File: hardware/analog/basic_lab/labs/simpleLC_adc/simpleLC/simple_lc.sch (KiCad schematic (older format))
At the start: 5 parts, among them J2 Conn_01x02_Male, Q2 BC547

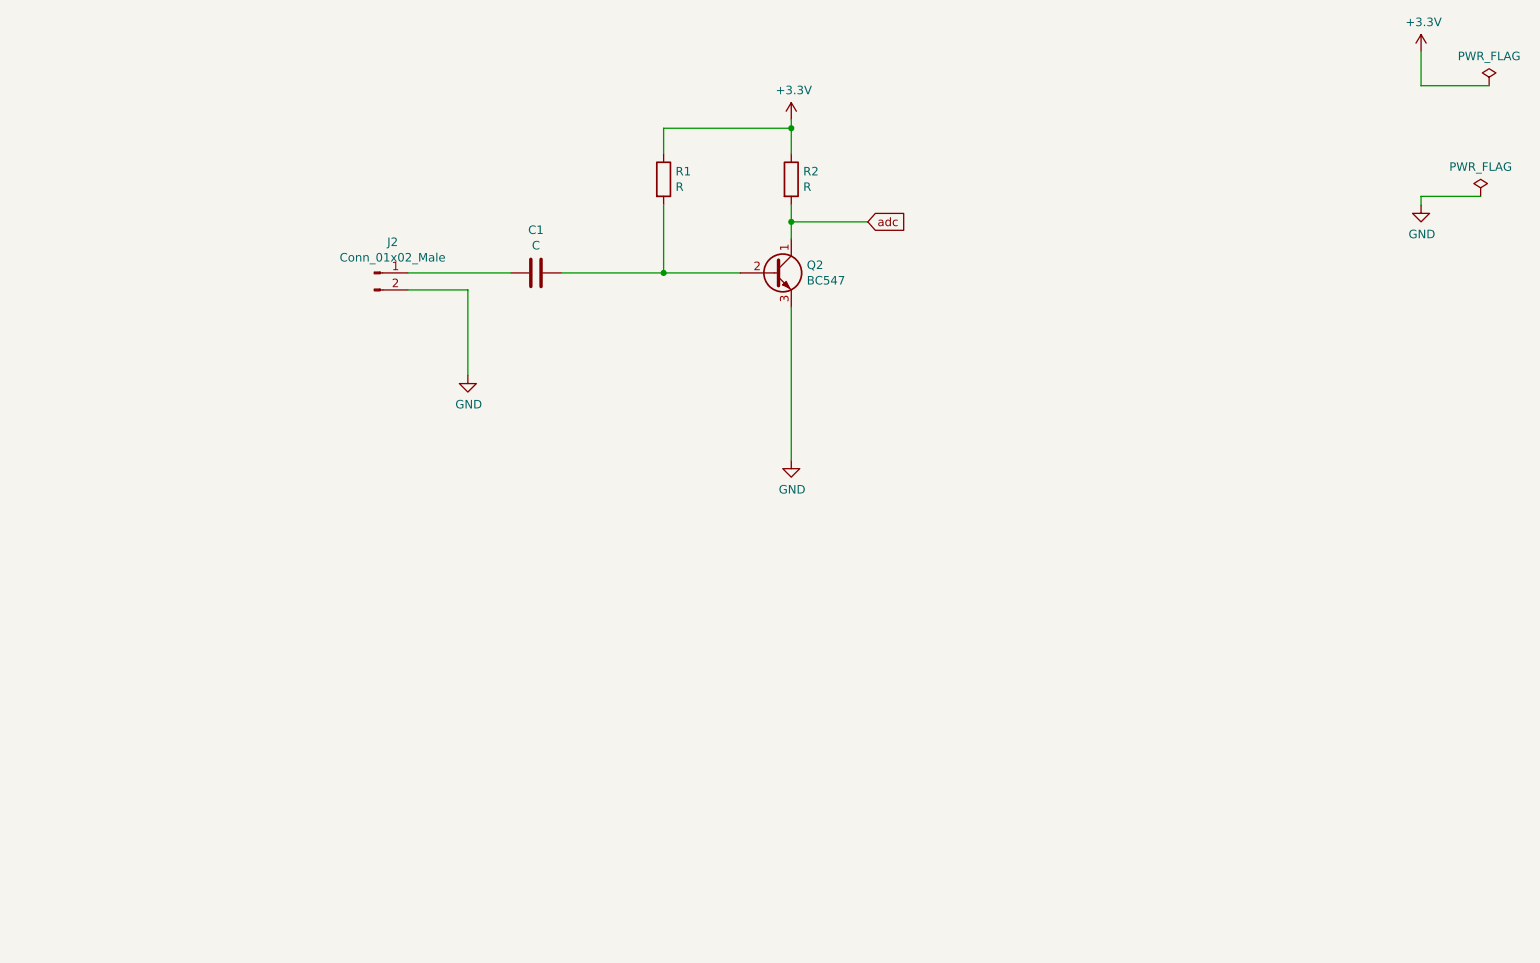
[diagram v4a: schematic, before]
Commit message: pwm => adc: started amplifier PCB
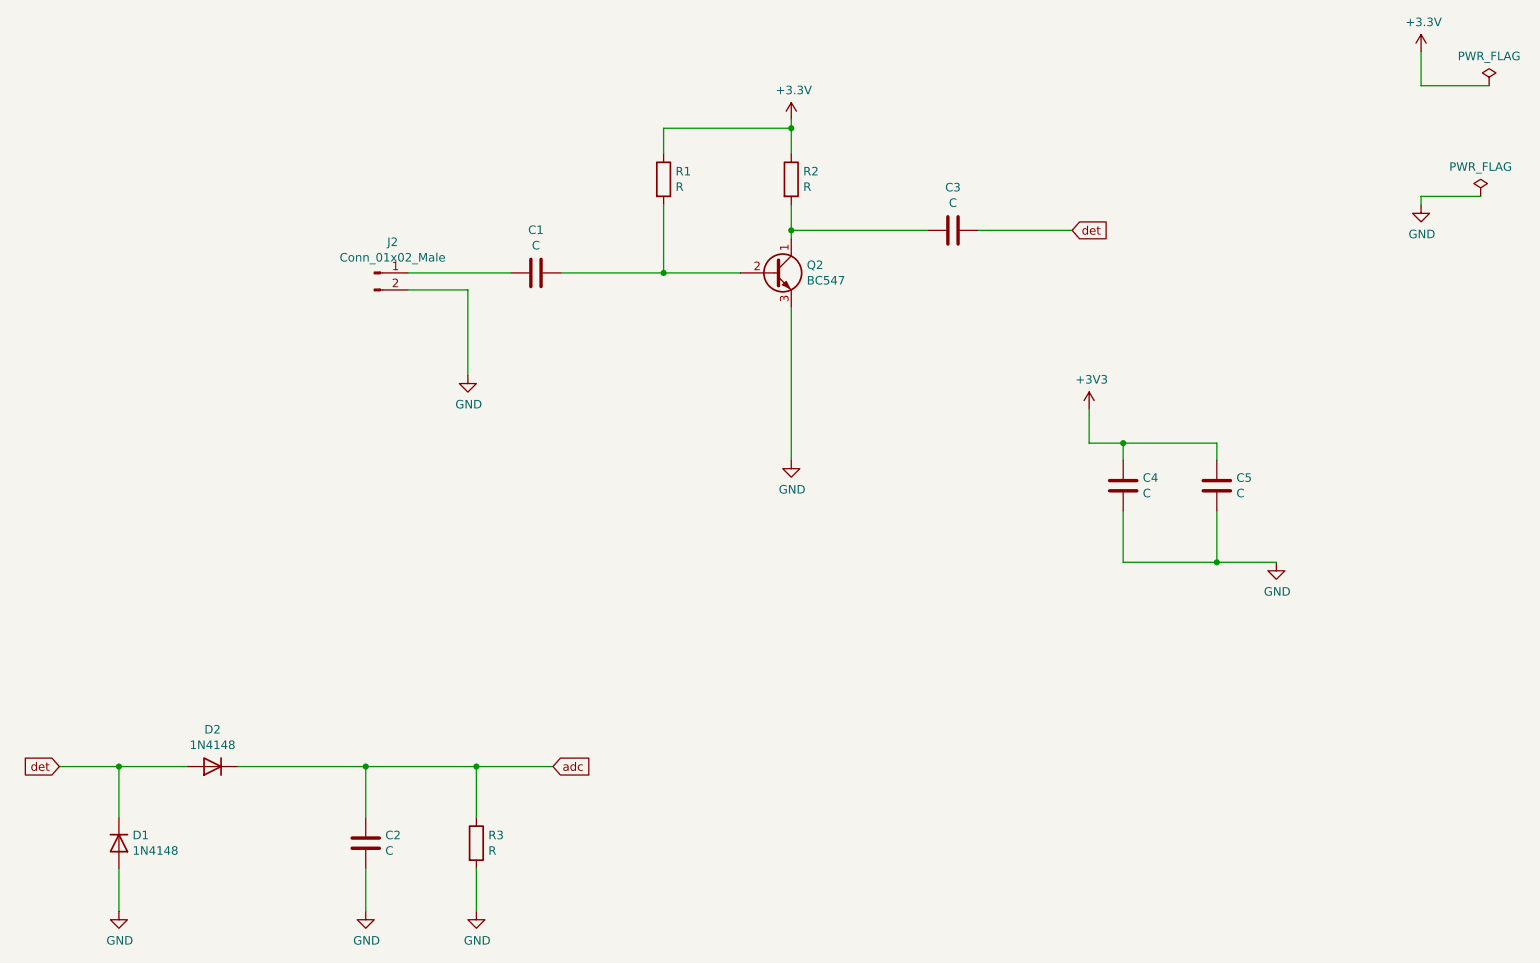
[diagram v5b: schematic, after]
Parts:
- added C2, C3, C4, C5: C, Capacitor_THT:C_Axial_L12.0mm_D6.5mm_P15.00mm_Horizontal, symbol Device:C
- added D1, D2: 1N4148, Diode_THT:D_DO-35_SOD27_P7.62mm_Horizontal, symbol Diode:1N4148
- added R3: R, Resistor_THT:R_Axial_DIN0309_L9.0mm_D3.2mm_P12.70mm_Horizontal, symbol Device:R
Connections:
- net +3V3: now also C4.1, C5.1
- net GND: now also C2.2, C4.2, C5.2, D1.2 (A), R3.2
- net adc: now also C2.1, D2.1 (K), R3.1; no longer Q2.1 (C), R2.2
- new net: C3.2, Q2.1 (C), R2.2
- new net det: C3.1, D1.1 (K), D2.2 (A)
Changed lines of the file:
@@
 $EndComp
-Wire Wire Line
-	6300 2350 6300 2250
 Wire Wire Line
 	6300 1850 6300 1700
@@
 Wire Wire Line
 	5550 2550 6000 2550
-Text GLabel 6750 2250 2    50   Input ~ 0
+Text GLabel 4900 5450 2    50   Input ~ 0
 adc
 Wire Wire Line
-	6300 2250 6750 2250
-Connection ~ 6300 2250
-Wire Wire Line
-	6300 2250 6300 2150
+	4450 5450 4900 5450
 $Comp
 L Device:C C1
@@
 Wire Wire Line
 	4050 2550 4650 2550
+Wire Wire Line
+	6300 2150 6300 2300
+$Comp
+L Device:C C3
+U 1 1 60FBF41C
+P 7250 2300
+F 0 "C3" V 6998 2300 50  0000 C CNN
+F 1 "C" V 7089 2300 50  0000 C CNN
+F 2 "Capacitor_THT:C_Axial_L12.0mm_D6.5mm_P15.00mm_Horizontal" H 7288 2150 50  0001 C CNN
+F 3 "~" H 7250 2300 50  0001 C CNN
+	1    7250 2300
+	0    1    1    0
+$EndComp
+Wire Wire Line
+	6300 2300 7100 2300
+Connection ~ 6300 2300
+Wire Wire Line
+	6300 2300 6300 2350
+Text GLabel 7950 2300 2    50   Input ~ 0
+det
+Wire Wire Line
+	7400 2300 7950 2300
+Text GLabel 2000 5450 0    50   Input ~ 0
+det
+$Comp
+L Diode:1N4148 D1
+U 1 1 60FC0E20
+P 2350 5900
+F 0 "D1" V 2304 5980 50  0000 L CNN
+F 1 "1N4148" V 2395 5980 50  0000 L CNN
+F 2 "Diode_THT:D_DO-35_SOD27_P7.62mm_Horizontal" H 2350 5725 50  0001 C CNN
+F 3 "https://assets.nexperia.com/documents/data-sheet/1N4148_1N4448.pdf" H 2350 5900 50  0001 C CNN
+	1    2350 5900
+	0    1    1    0
+$EndComp
+$Comp
+L Diode:1N4148 D2
+U 1 1 60FC14E5
+P 2900 5450
+F 0 "D2" H 2900 5233 50  0000 C CNN
+F 1 "1N4148" H 2900 5324 50  0000 C CNN
+F 2 "Diode_THT:D_DO-35_SOD27_P7.62mm_Horizontal" H 2900 5275 50  0001 C CNN
+F 3 "https://assets.nexperia.com/documents/data-sheet/1N4148_1N4448.pdf" H 2900 5450 50  0001 C CNN
+	1    2900 5450
+	-1   0    0    1
+$EndComp
+$Comp
+L Device:C C2
+U 1 1 60FC1C5C
+P 3800 5900
+F 0 "C2" H 3915 5946 50  0000 L CNN
+F 1 "C" H 3915 5855 50  0000 L CNN
+F 2 "Capacitor_THT:C_Axial_L12.0mm_D6.5mm_P15.00mm_Horizontal" H 3838 5750 50  0001 C CNN
+F 3 "~" H 3800 5900 50  0001 C CNN
+	1    3800 5900
+	1    0    0    -1
+$EndComp
+$Comp
+L Device:R R3
+U 1 1 60FC20D4
+P 4450 5900
+F 0 "R3" H 4520 5946 50  0000 L CNN
+F 1 "R" H 4520 5855 50  0000 L CNN
+F 2 "Resistor_THT:R_Axial_DIN0309_L9.0mm_D3.2mm_P12.70mm_Horizontal" V 4380 5900 50  0001 C CNN
+F 3 "~" H 4450 5900 50  0001 C CNN
+	1    4450 5900
+	1    0    0    -1
+$EndComp
+Wire Wire Line
+	2000 5450 2350 5450
+Wire Wire Line
+	2350 5750 2350 5450
+Connection ~ 2350 5450
+Wire Wire Line
+	2350 5450 2750 5450
+Wire Wire Line
+	3050 5450 3800 5450
+Wire Wire Line
+	4450 5450 4450 5750
+Wire Wire Line
+	3800 5750 3800 5450
+Connection ~ 3800 5450
+Wire Wire Line
+	3800 5450 4450 5450
+$Comp
+L power:GND #PWR04
+U 1 1 60FC6783
+P 2350 6300
+F 0 "#PWR04" H 2350 6050 50  0001 C CNN
+F 1 "GND" H 2355 6127 50  0000 C CNN
+F 2 "" H 2350 6300 50  0001 C CNN
+F 3 "" H 2350 6300 50  0001 C CNN
+	1    2350 6300
+	1    0    0    -1
+$EndComp
+Wire Wire Line
+	2350 6050 2350 6300
+$Comp
+L power:GND #PWR05
+U 1 1 60FC9E23
+P 3800 6300
+F 0 "#PWR05" H 3800 6050 50  0001 C CNN
+F 1 "GND" H 3805 6127 50  0000 C CNN
+F 2 "" H 3800 6300 50  0001 C CNN
+F 3 "" H 3800 6300 50  0001 C CNN
+	1    3800 6300
+	1    0    0    -1
+$EndComp
+Wire Wire Line
+	3800 6050 3800 6300
+$Comp
+L power:GND #PWR06
+U 1 1 60FCA625
+P 4450 6300
+F 0 "#PWR06" H 4450 6050 50  0001 C CNN
+F 1 "GND" H 4455 6127 50  0000 C CNN
+F 2 "" H 4450 6300 50  0001 C CNN
+F 3 "" H 4450 6300 50  0001 C CNN
+	1    4450 6300
+	1    0    0    -1
+$EndComp
+Wire Wire Line
+	4450 6050 4450 6300
+Connection ~ 4450 5450
+$Comp
+L power:+3V3 #PWR07
+U 1 1 60FD5413
+P 8050 3350
+F 0 "#PWR07" H 8050 3200 50  0001 C CNN
+F 1 "+3V3" H 8065 3523 50  0000 C CNN
+F 2 "" H 8050 3350 50  0001 C CNN
+F 3 "" H 8050 3350 50  0001 C CNN
+	1    8050 3350
+	1    0    0    -1
+$EndComp
+$Comp
+L power:GND #PWR08
+U 1 1 60FD5BF2
+P 9150 4250
+F 0 "#PWR08" H 9150 4000 50  0001 C CNN
+F 1 "GND" H 9155 4077 50  0000 C CNN
+F 2 "" H 9150 4250 50  0001 C CNN
+F 3 "" H 9150 4250 50  0001 C CNN
+	1    9150 4250
+	1    0    0    -1
+$EndComp
+$Comp
+L Device:C C4
+U 1 1 60FD612F
+P 8250 3800
+F 0 "C4" H 8365 3846 50  0000 L CNN
+F 1 "C" H 8365 3755 50  0000 L CNN
+F 2 "Capacitor_THT:C_Axial_L12.0mm_D6.5mm_P15.00mm_Horizontal" H 8288 3650 50  0001 C CNN
+F 3 "~" H 8250 3800 50  0001 C CNN
+	1    8250 3800
+	1    0    0    -1
+$EndComp
+$Comp
+L Device:C C5
+U 1 1 60FD67A1
+P 8800 3800
+F 0 "C5" H 8915 3846 50  0000 L CNN
+F 1 "C" H 8915 3755 50  0000 L CNN
+F 2 "Capacitor_THT:C_Axial_L12.0mm_D6.5mm_P15.00mm_Horizontal" H 8838 3650 50  0001 C CNN
+F 3 "~" H 8800 3800 50  0001 C CNN
+	1    8800 3800
+	1    0    0    -1
+$EndComp
+Wire Wire Line
+	8050 3350 8050 3550
+Wire Wire Line
+	8050 3550 8250 3550
+Wire Wire Line
+	8800 3550 8800 3650
+Wire Wire Line
+	8250 3550 8250 3650
+Connection ~ 8250 3550
+Wire Wire Line
+	8250 3550 8800 3550
+Wire Wire Line
+	8250 3950 8250 4250
+Wire Wire Line
+	8250 4250 8800 4250
+Wire Wire Line
+	8800 3950 8800 4250
+Connection ~ 8800 4250
+Wire Wire Line
+	8800 4250 9150 4250
 $EndSCHEMATC
